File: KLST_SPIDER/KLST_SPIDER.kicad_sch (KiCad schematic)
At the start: 25 parts, among them J1 MIDI_IN, J10 UART, J11 UART, J12 UART, J13 MIDI_OUT, J2 MIDI_OUT, J3 UART, J4 UART, J5 UART, J6 UART, J7 UART, J8 UART, J9 UART, U1 H11L1, U2 74AHC1G125, U3 74AHC1G125

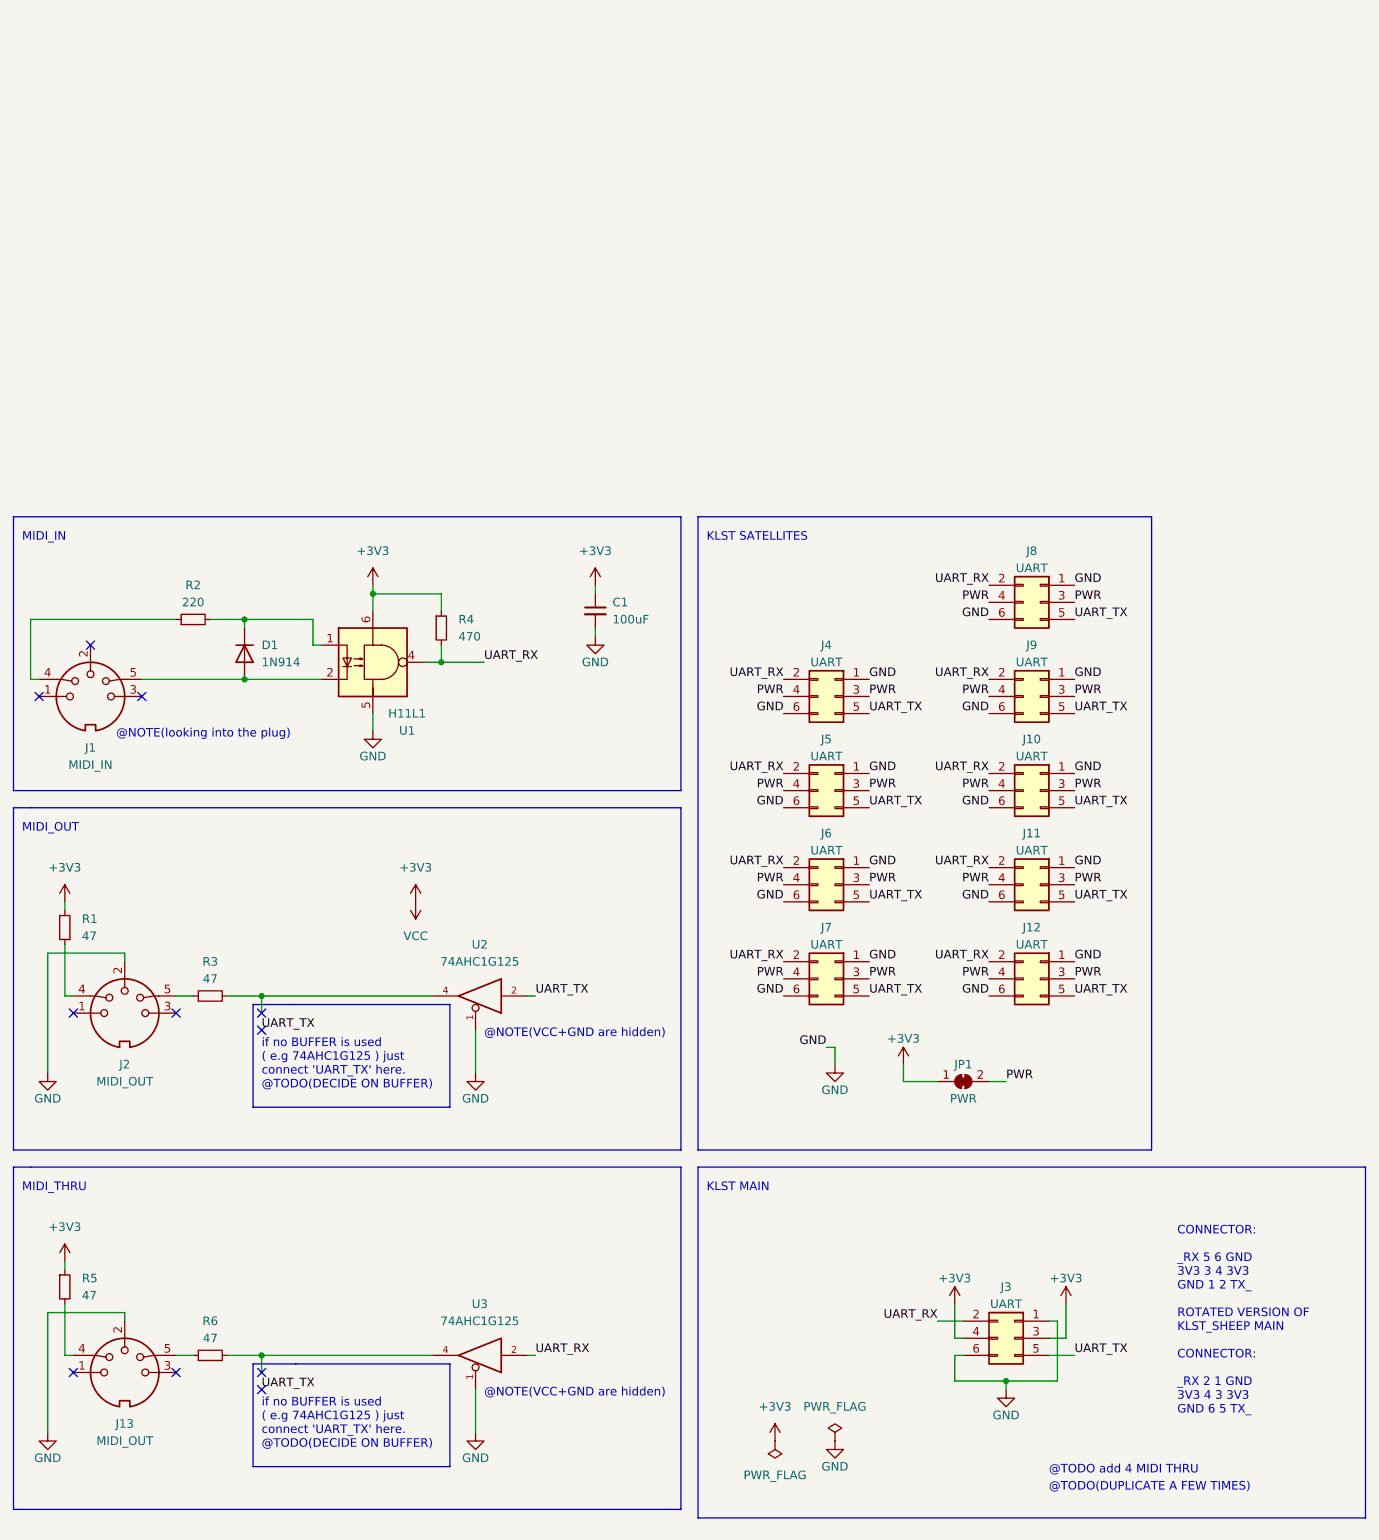
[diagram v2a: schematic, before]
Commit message: rearranged connectors
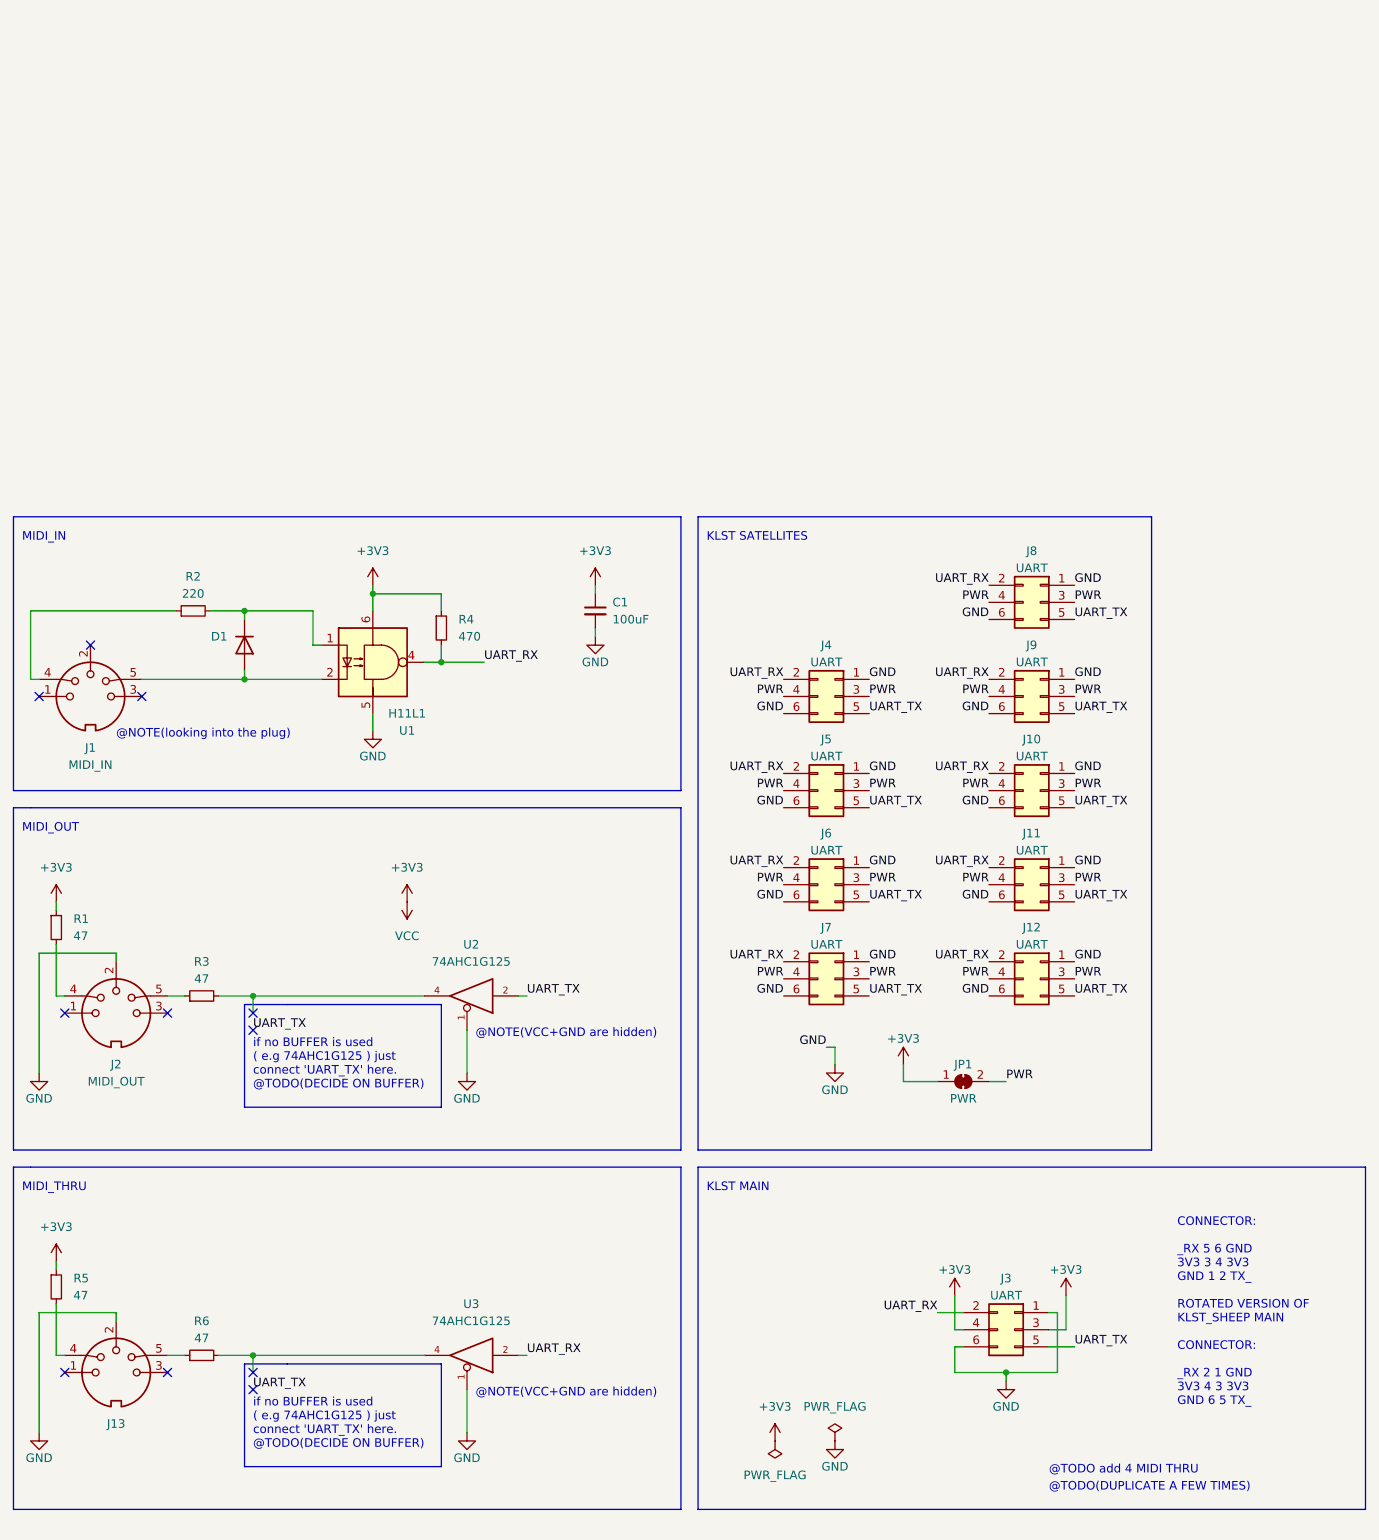
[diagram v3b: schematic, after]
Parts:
- removed D1: 1N914, Diode_THT:D_DO-35_SOD27_P7.62mm_Horizontal, symbol Diode:1N914
- added D1: (no value), symbol Diode:1N914WT
- J1, J2: footprint (none) -> DIN-5:DIN5-RA-PTH
- J13: value MIDI_OUT -> (none)
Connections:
- net at R2.2, U1.1: now also D1.1 (K)
- net at J1.5, U1.2: now also D1.2 (A)
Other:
- moved on the sheet: J13, J2, J3, R1, R2, R3, R5, R6, U2, U3

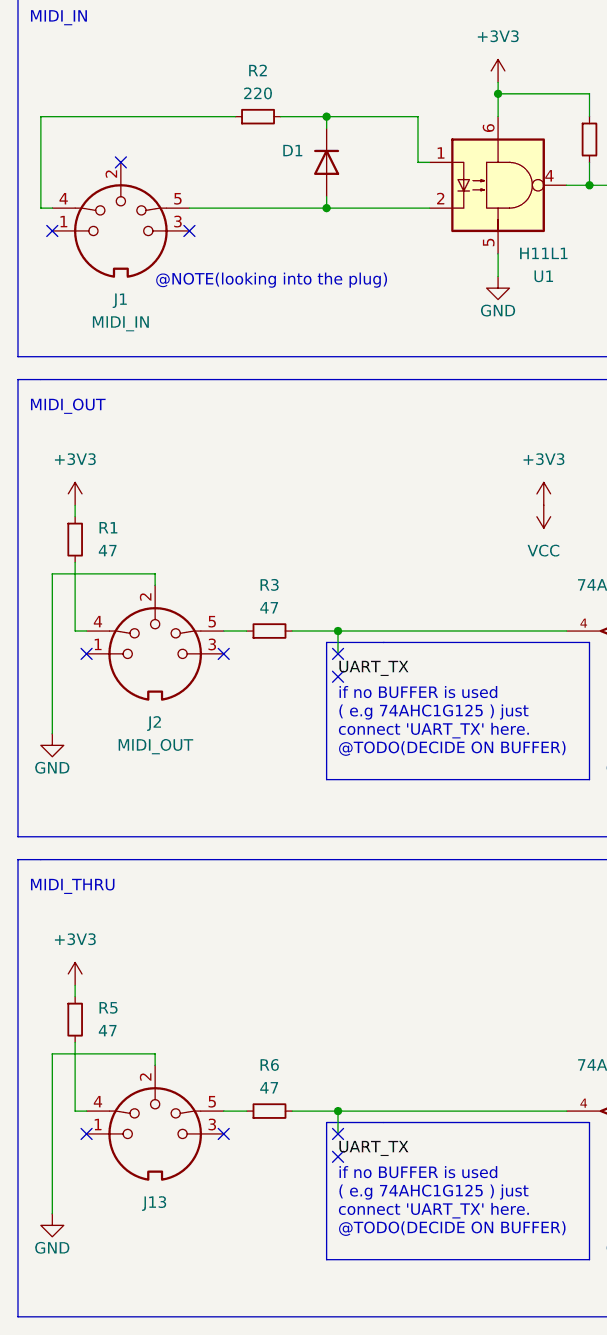
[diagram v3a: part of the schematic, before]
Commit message: rearranged connectors
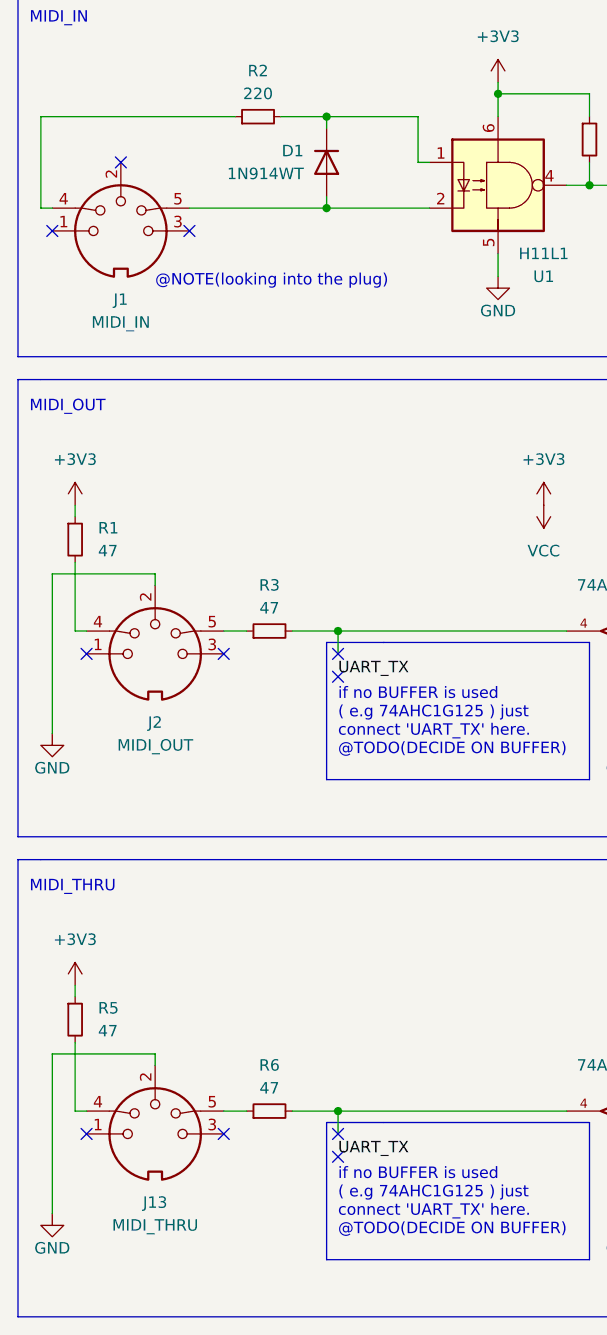
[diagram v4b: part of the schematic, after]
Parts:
- D1: value (none) -> 1N914WT; footprint (none) -> Diode_SMD:D_SOD-523
- J13: value (none) -> MIDI_THRU
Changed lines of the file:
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@@
     (in_bom yes) (on_board yes) (fields_autoplaced)
     (property "Reference" "J13" (id 0) (at 29.2101 148.59 0))
-    (property "Value" "" (id 1) (at 29.2101 151.13 0))
+    (property "Value" "MIDI_THRU" (id 1) (at 29.2101 151.13 0))
     (property "Footprint" "DIN-5:DIN5-RA-PTH" (id 2) (at 29.21 140.97 0)
       (effects (font (size 1.27 1.27)) hide)
@@
       (effects (font (size 1.27 1.27)) (justify right))
     )
-    (property "Value" "" (id 1) (at 45.72 34.29 90)
+    (property "Value" "1N914WT" (id 1) (at 45.72 34.29 90)
       (effects (font (size 1.27 1.27)) (justify right))
     )
-    (property "Footprint" "" (id 2) (at 43.815 33.02 0)
+    (property "Footprint" "Diode_SMD:D_SOD-523" (id 2) (at 43.815 33.02 0)
       (effects (font (size 1.27 1.27)) hide)
     )

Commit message: prepared JLPCPB production
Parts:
- removed J1: MIDI_IN, DIN-5:DIN5-RA-PTH, symbol Connector:DIN-5_180degree
- removed J10, J11, J12, J4, J5, J6, J7, J8, J9: UART, Connector_IDC:IDC-Header_2x03_P2.54mm_Horizontal, symbol Connector_Generic:Conn_02x03_Odd_Even
- removed J13: MIDI_THRU, DIN-5:DIN5-RA-PTH, symbol Connector:DIN-5_180degree
- removed J2: MIDI_OUT, DIN-5:DIN5-RA-PTH, symbol Connector:DIN-5_180degree
- added J1, J2, J3: (no value), symbol Connector:DIN-5_180degree_with_Eaerth
- C1: value 100uF -> (none); footprint Capacitor_SMD:C_0805_2012Metric_Pad1.18x1.45mm_HandSolder -> (none); Extended Part (none) -> -; JLCPCB Part # (none) -> C696821; MPN (none) -> F380G107MSALZT
- D1: value 1N914WT -> (none); footprint Diode_SMD:D_SOD-523 -> (none); Extended Part (none) -> -; JLCPCB Part # (none) -> C896167; MPN (none) -> 1N914BWT
- J4: renamed from J3; value UART -> (none); footprint Connector_IDC:IDC-Header_2x03_P2.54mm_Horizontal -> (none)
- JP1: value PWR -> (none); footprint Jumper:SolderJumper-2_P1.3mm_Bridged_RoundedPad1.0x1.5mm -> (none); JLCPCB Part # (none) -> -
- R1: value 47 -> (none); footprint Resistor_SMD:R_0805_2012Metric_Pad1.20x1.40mm_HandSolder -> (none); Extended Part (none) -> -; JLCPCB Part # (none) -> C328398
- R2: renamed from R5; value 47 -> (none); footprint Resistor_SMD:R_0805_2012Metric_Pad1.20x1.40mm_HandSolder -> (none); Extended Part (none) -> -; JLCPCB Part # (none) -> C328398
- R3: renamed from R2; value 220 -> (none); footprint Resistor_SMD:R_0805_2012Metric_Pad1.20x1.40mm_HandSolder -> (none); Extended Part (none) -> -; JLCPCB Part # (none) -> C479094
- R4: renamed from R3; value 47 -> (none); footprint Resistor_SMD:R_0805_2012Metric_Pad1.20x1.40mm_HandSolder -> (none); Extended Part (none) -> -; JLCPCB Part # (none) -> C328398
- R5: renamed from R6; value 47 -> (none); footprint Resistor_SMD:R_0805_2012Metric_Pad1.20x1.40mm_HandSolder -> (none); Extended Part (none) -> -; JLCPCB Part # (none) -> C328398
- R6: renamed from R4; value 470 -> (none); footprint Resistor_SMD:R_0805_2012Metric_Pad1.20x1.40mm_HandSolder -> (none); Extended Part (none) -> -; JLCPCB Part # (none) -> C328396
- U1: value H11L1 -> (none); footprint Package_DIP:SMDIP-6_W9.53mm -> (none); Extended Part (none) -> -; JLCPCB Part # (none) -> C20082
- U2, U3: value 74AHC1G125 -> (none); footprint Package_TO_SOT_SMD:SOT-23-5_HandSoldering -> (none); Extended Part (none) -> -; JLCPCB Part # (none) -> C7468
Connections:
- net GND: now also J2.2, J3.2
- net at R2.2: now also J3.4
- net at R5.1: now also J3.5
- net at R1.2: now also J2.4
- net at D1.2 (A), U1.2: now also J1.5
- net at R4.1: now also J2.5
- net at R3.1: now also J1.4
- no-connect marks 11 -> 17
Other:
- added sheet KLST_01 (klst_satellite.kicad_sch)
- added sheet KLST_02 (klst_satellite.kicad_sch)
- added sheet KLST_03 (klst_satellite.kicad_sch)
- added sheet KLST_04 (klst_satellite.kicad_sch)
- added sheet KLST_05 (klst_satellite.kicad_sch)
- added sheet KLST_06 (klst_satellite.kicad_sch)
- added sheet KLST_07 (klst_satellite.kicad_sch)
- added sheet KLST_08 (klst_satellite.kicad_sch)
- added sheet KLST_09 (klst_satellite.kicad_sch)
- note removed: "@TODO add 4 MIDI THRU"
- note removed: "@TODO(DUPLICATE A FEW TIMES)"
- moved on the sheet: C1, D1, J4, JP1
